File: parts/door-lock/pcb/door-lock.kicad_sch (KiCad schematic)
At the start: 6 parts, among them J2 RJ45_Shielded, U1 L293D

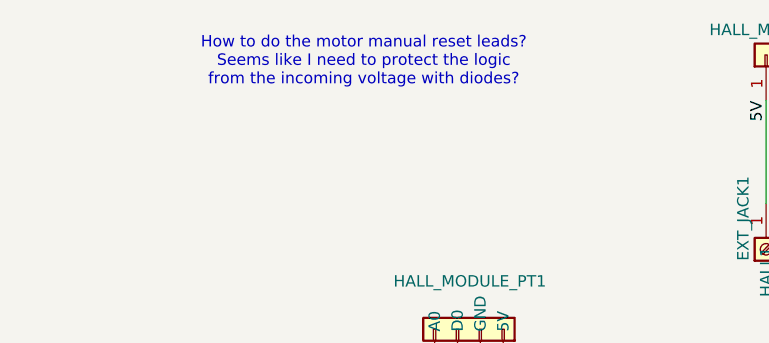
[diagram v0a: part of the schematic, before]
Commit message: pcb revisions to update to better RJ45 jack, update QR code.
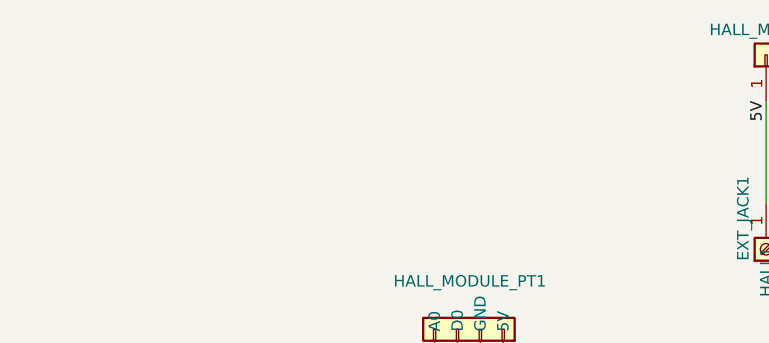
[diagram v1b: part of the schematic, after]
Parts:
- J2: footprint Connector_RJ:RJ45_Ninigi_GE -> Connector_RJ:RJ45_Amphenol_RJHSE5380
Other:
- note removed: "How to do the motor manual reset leads? Seems like I need to protect the logic from the incoming voltage with diodes?"
